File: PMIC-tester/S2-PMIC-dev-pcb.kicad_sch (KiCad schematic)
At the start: 25 parts, among them J1 USB_C_Receptacle_USB2.0, P1 CONN_02X13, P3 CONN_02X13, SW1 RESET, SW2 BOOT, U1 MCP1700-1202E_SOT23, U2 ESP32-S2-WROVER, U3 TPS65185RGZR

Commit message: DRC
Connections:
- net IO36: now also P3.22 (Pin_22)
- net IO37: now also P3.24 (Pin_24)
- no-connect marks 48 -> 46
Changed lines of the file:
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@@
   (no_connect (at 153.67 138.43))
   (no_connect (at 176.53 153.67))
-  (no_connect (at 191.77 135.89))
-  (no_connect (at 194.31 135.89))
   (no_connect (at 83.82 92.71))
   (no_connect (at 83.82 57.15))
@@
     (stroke (width 0) (type default) (color 0 0 0 0))
   )
+  (wire (pts (xy 83.82 64.77) (xy 86.36 64.77))
+    (stroke (width 0) (type default) (color 0 0 0 0))
+  )
+  (wire (pts (xy 120.65 64.77) (xy 116.84 64.77))
+    (stroke (width 0) (type default) (color 0 0 0 0))
+  )
+  (wire (pts (xy 269.24 77.47) (xy 269.24 68.58))
+    (stroke (width 0) (type default) (color 0 0 0 0))
+  )
+  (wire (pts (xy 149.86 106.68) (xy 119.38 106.68))
+    (stroke (width 0) (type default) (color 0 0 0 0))
+  )
+  (wire (pts (xy 120.65 82.55) (xy 116.84 82.55))
+    (stroke (width 0) (type default) (color 0 0 0 0))
+  )
+  (wire (pts (xy 176.53 135.89) (xy 176.53 138.43))
+    (stroke (width 0) (type default) (color 0 0 0 0))
+  )
   (wire (pts (xy 191.77 135.89) (xy 191.77 138.43))
     (stroke (width 0) (type default) (color 0 0 0 0))
   )
-  (wire (pts (xy 83.82 64.77) (xy 86.36 64.77))
-    (stroke (width 0) (type default) (color 0 0 0 0))
-  )
-  (wire (pts (xy 120.65 64.77) (xy 116.84 64.77))
-    (stroke (width 0) (type default) (color 0 0 0 0))
-  )
-  (wire (pts (xy 269.24 77.47) (xy 269.24 68.58))
-    (stroke (width 0) (type default) (color 0 0 0 0))
-  )
-  (wire (pts (xy 149.86 106.68) (xy 119.38 106.68))
-    (stroke (width 0) (type default) (color 0 0 0 0))
-  )
-  (wire (pts (xy 120.65 82.55) (xy 116.84 82.55))
-    (stroke (width 0) (type default) (color 0 0 0 0))
-  )
-  (wire (pts (xy 176.53 135.89) (xy 176.53 138.43))
-    (stroke (width 0) (type default) (color 0 0 0 0))
-  )
   (wire (pts (xy 140.97 116.84) (xy 143.51 116.84))
     (stroke (width 0) (type default) (color 0 0 0 0))
@@
     (stroke (width 0) (type default) (color 0 0 0 0))
   )
+  (wire (pts (xy 256.54 34.29) (xy 262.89 34.29))
+    (stroke (width 0) (type default) (color 0 0 0 0))
+  )
+  (wire (pts (xy 83.82 77.47) (xy 86.36 77.47))
+    (stroke (width 0) (type default) (color 0 0 0 0))
+  )
+  (wire (pts (xy 171.45 151.13) (xy 171.45 161.29))
+    (stroke (width 0) (type default) (color 0 0 0 0))
+  )
+  (wire (pts (xy 120.65 44.45) (xy 116.84 44.45))
+    (stroke (width 0) (type default) (color 0 0 0 0))
+  )
+  (wire (pts (xy 83.82 80.01) (xy 86.36 80.01))
+    (stroke (width 0) (type default) (color 0 0 0 0))
+  )
+  (wire (pts (xy 166.37 135.89) (xy 166.37 138.43))
+    (stroke (width 0) (type default) (color 0 0 0 0))
+  )
+  (wire (pts (xy 160.02 41.91) (xy 162.56 41.91))
+    (stroke (width 0) (type default) (color 0 0 0 0))
+  )
+  (wire (pts (xy 83.82 59.69) (xy 86.36 59.69))
+    (stroke (width 0) (type default) (color 0 0 0 0))
+  )
+  (wire (pts (xy 83.82 54.61) (xy 86.36 54.61))
+    (stroke (width 0) (type default) (color 0 0 0 0))
+  )
+  (wire (pts (xy 120.65 132.08) (xy 120.65 161.29))
+    (stroke (width 0) (type default) (color 0 0 0 0))
+  )
+  (wire (pts (xy 120.65 74.93) (xy 116.84 74.93))
+    (stroke (width 0) (type default) (color 0 0 0 0))
+  )
+  (wire (pts (xy 140.97 92.71) (xy 140.97 100.33))
+    (stroke (width 0) (type default) (color 0 0 0 0))
+  )
+  (wire (pts (xy 196.85 153.67) (xy 196.85 151.13))
+    (stroke (width 0) (type default) (color 0 0 0 0))
+  )
+  (wire (pts (xy 120.65 57.15) (xy 116.84 57.15))
+    (stroke (width 0) (type default) (color 0 0 0 0))
+  )
+  (wire (pts (xy 83.82 82.55) (xy 86.36 82.55))
+    (stroke (width 0) (type default) (color 0 0 0 0))
+  )
+  (wire (pts (xy 196.85 135.89) (xy 196.85 138.43))
+    (stroke (width 0) (type default) (color 0 0 0 0))
+  )
+  (wire (pts (xy 120.65 161.29) (xy 171.45 161.29))
+    (stroke (width 0) (type default) (color 0 0 0 0))
+  )
+  (wire (pts (xy 254 113.03) (xy 254 115.57))
+    (stroke (width 0) (type default) (color 0 0 0 0))
+  )
+  (wire (pts (xy 269.24 33.02) (xy 274.32 33.02))
+    (stroke (width 0) (type default) (color 0 0 0 0))
+  )
+  (wire (pts (xy 149.86 88.9) (xy 149.86 106.68))
+    (stroke (width 0) (type default) (color 0 0 0 0))
+  )
+  (wire (pts (xy 166.37 153.67) (xy 166.37 151.13))
+    (stroke (width 0) (type default) (color 0 0 0 0))
+  )
+  (polyline (pts (xy 176.53 26.67) (xy 138.43 26.67))
+    (stroke (width 0) (type default) (color 0 0 0 0))
+  )
   (wire (pts (xy 194.31 135.89) (xy 194.31 138.43))
-    (stroke (width 0) (type default) (color 0 0 0 0))
-  )
-  (wire (pts (xy 256.54 34.29) (xy 262.89 34.29))
-    (stroke (width 0) (type default) (color 0 0 0 0))
-  )
-  (wire (pts (xy 83.82 77.47) (xy 86.36 77.47))
-    (stroke (width 0) (type default) (color 0 0 0 0))
-  )
-  (wire (pts (xy 171.45 151.13) (xy 171.45 161.29))
-    (stroke (width 0) (type default) (color 0 0 0 0))
-  )
-  (wire (pts (xy 120.65 44.45) (xy 116.84 44.45))
-    (stroke (width 0) (type default) (color 0 0 0 0))
-  )
-  (wire (pts (xy 83.82 80.01) (xy 86.36 80.01))
-    (stroke (width 0) (type default) (color 0 0 0 0))
-  )
-  (wire (pts (xy 166.37 135.89) (xy 166.37 138.43))
-    (stroke (width 0) (type default) (color 0 0 0 0))
-  )
-  (wire (pts (xy 160.02 41.91) (xy 162.56 41.91))
-    (stroke (width 0) (type default) (color 0 0 0 0))
-  )
-  (wire (pts (xy 83.82 59.69) (xy 86.36 59.69))
-    (stroke (width 0) (type default) (color 0 0 0 0))
-  )
-  (wire (pts (xy 83.82 54.61) (xy 86.36 54.61))
-    (stroke (width 0) (type default) (color 0 0 0 0))
-  )
-  (wire (pts (xy 120.65 132.08) (xy 120.65 161.29))
-    (stroke (width 0) (type default) (color 0 0 0 0))
-  )
-  (wire (pts (xy 120.65 74.93) (xy 116.84 74.93))
-    (stroke (width 0) (type default) (color 0 0 0 0))
-  )
-  (wire (pts (xy 140.97 92.71) (xy 140.97 100.33))
-    (stroke (width 0) (type default) (color 0 0 0 0))
-  )
-  (wire (pts (xy 196.85 153.67) (xy 196.85 151.13))
-    (stroke (width 0) (type default) (color 0 0 0 0))
-  )
-  (wire (pts (xy 120.65 57.15) (xy 116.84 57.15))
-    (stroke (width 0) (type default) (color 0 0 0 0))
-  )
-  (wire (pts (xy 83.82 82.55) (xy 86.36 82.55))
-    (stroke (width 0) (type default) (color 0 0 0 0))
-  )
-  (wire (pts (xy 196.85 135.89) (xy 196.85 138.43))
-    (stroke (width 0) (type default) (color 0 0 0 0))
-  )
-  (wire (pts (xy 120.65 161.29) (xy 171.45 161.29))
-    (stroke (width 0) (type default) (color 0 0 0 0))
-  )
-  (wire (pts (xy 254 113.03) (xy 254 115.57))
-    (stroke (width 0) (type default) (color 0 0 0 0))
-  )
-  (wire (pts (xy 269.24 33.02) (xy 274.32 33.02))
-    (stroke (width 0) (type default) (color 0 0 0 0))
-  )
-  (wire (pts (xy 149.86 88.9) (xy 149.86 106.68))
-    (stroke (width 0) (type default) (color 0 0 0 0))
-  )
-  (wire (pts (xy 166.37 153.67) (xy 166.37 151.13))
-    (stroke (width 0) (type default) (color 0 0 0 0))
-  )
-  (polyline (pts (xy 176.53 26.67) (xy 138.43 26.67))
     (stroke (width 0) (type default) (color 0 0 0 0))
   )
@@
     (effects (font (size 1.27 1.27)) (justify left bottom))
   )
+  (label "IO37" (at 194.31 135.89 90)
+    (effects (font (size 1.27 1.27)) (justify left bottom))
+  )
   (label "3.3V" (at 218.44 80.01 180)
     (effects (font (size 1.27 1.27)) (justify right bottom))
@@
     (effects (font (size 1.27 1.27)) (justify left bottom))
   )
+  (label "IO36" (at 191.77 135.89 90)
+    (effects (font (size 1.27 1.27)) (justify left bottom))
+  )

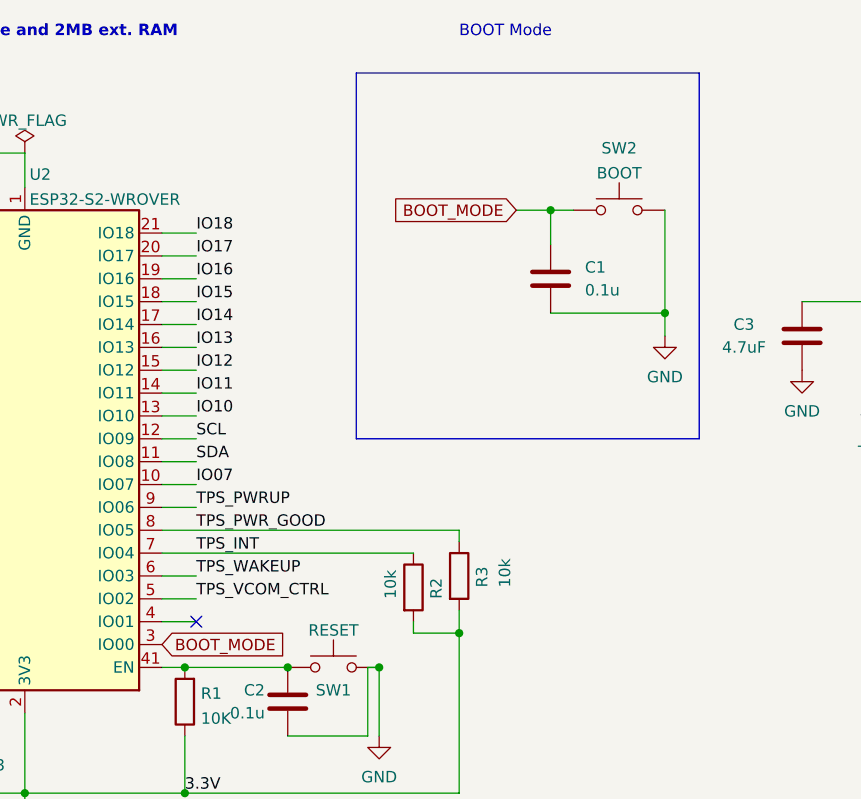
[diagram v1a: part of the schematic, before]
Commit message: I2C pullups
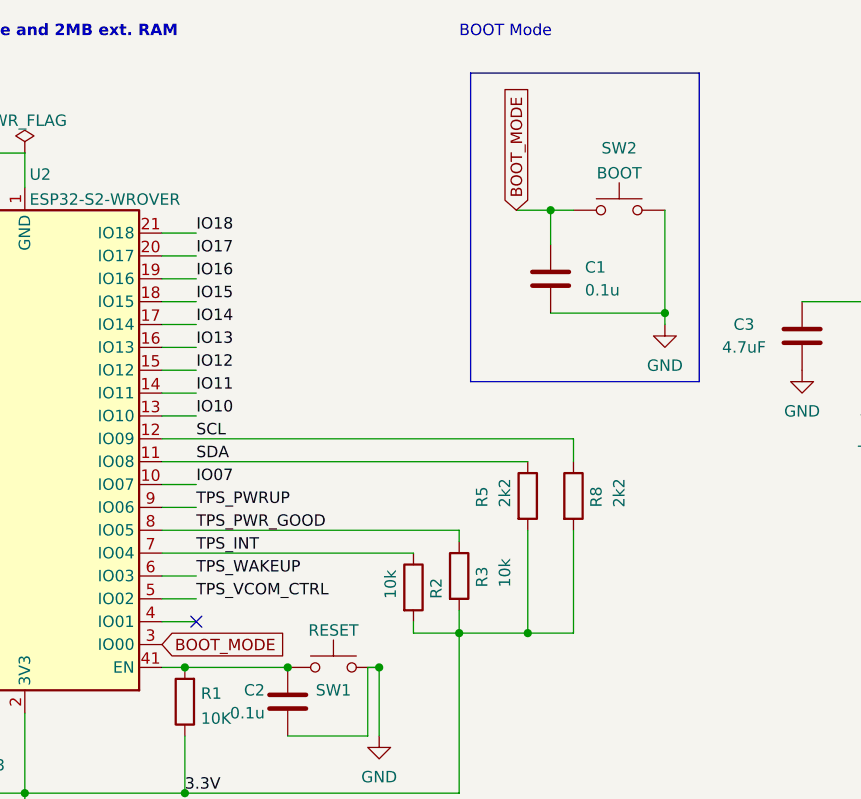
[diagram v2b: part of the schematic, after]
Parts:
- added R5, R8: 2k2, Resistor_SMD:R_0603_1608Metric, symbol Device:R
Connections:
- net 3.3V: now also R5.2, R8.2
- net SCL: now also R8.1
- net SDA: now also R5.1
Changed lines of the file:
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@@
   (junction (at 172.72 53.34) (diameter 0) (color 0 0 0 0)
+  )
+  (junction (at 157.48 88.9) (diameter 0) (color 0 0 0 0)
   )
   (junction (at 52.07 54.61) (diameter 0) (color 0 0 0 0)
@@
     (stroke (width 0) (type default) (color 0 0 0 0))
   )
+  (wire (pts (xy 162.56 67.31) (xy 162.56 69.85))
+    (stroke (width 0) (type default) (color 0 0 0 0))
+  )
   (wire (pts (xy 254 57.15) (xy 276.86 57.15))
     (stroke (width 0) (type default) (color 0 0 0 0))
@@
     (stroke (width 0) (type default) (color 0 0 0 0))
   )
+  (wire (pts (xy 157.48 77.47) (xy 157.48 88.9))
+    (stroke (width 0) (type default) (color 0 0 0 0))
+  )
   (wire (pts (xy 194.31 153.67) (xy 194.31 151.13))
     (stroke (width 0) (type default) (color 0 0 0 0))
@@
     (stroke (width 0) (type default) (color 0 0 0 0))
   )
-  (polyline (pts (xy 138.43 26.67) (xy 138.43 67.31))
+  (polyline (pts (xy 151.13 26.67) (xy 151.13 60.96))
     (stroke (width 0) (type default) (color 0 0 0 0))
   )
@@
     (stroke (width 0) (type default) (color 0 0 0 0))
   )
-  (wire (pts (xy 120.65 69.85) (xy 116.84 69.85))
+  (wire (pts (xy 116.84 69.85) (xy 157.48 69.85))
     (stroke (width 0) (type default) (color 0 0 0 0))
   )
@@
     (stroke (width 0) (type default) (color 0 0 0 0))
   )
+  (wire (pts (xy 162.56 88.9) (xy 157.48 88.9))
+    (stroke (width 0) (type default) (color 0 0 0 0))
+  )
   (wire (pts (xy 269.24 68.58) (xy 274.32 68.58))
     (stroke (width 0) (type default) (color 0 0 0 0))
@@
     (stroke (width 0) (type default) (color 0 0 0 0))
   )
+  (wire (pts (xy 162.56 77.47) (xy 162.56 88.9))
+    (stroke (width 0) (type default) (color 0 0 0 0))
+  )
   (wire (pts (xy 53.34 44.45) (xy 57.15 44.45))
     (stroke (width 0) (type default) (color 0 0 0 0))
@@
     (stroke (width 0) (type default) (color 0 0 0 0))
   )
-  (polyline (pts (xy 176.53 26.67) (xy 138.43 26.67))
+  (polyline (pts (xy 176.53 26.67) (xy 151.13 26.67))
     (stroke (width 0) (type default) (color 0 0 0 0))
   )
@@
     (stroke (width 0) (type default) (color 0 0 0 0))
   )
-  (polyline (pts (xy 138.43 67.31) (xy 176.53 67.31))
+  (polyline (pts (xy 151.13 60.96) (xy 176.53 60.96))
     (stroke (width 0) (type default) (color 0 0 0 0))
   )
@@
     (stroke (width 0) (type default) (color 0 0 0 0))
   )
-  (polyline (pts (xy 176.53 67.31) (xy 176.53 26.67))
+  (polyline (pts (xy 176.53 60.96) (xy 176.53 26.67))
     (stroke (width 0) (type default) (color 0 0 0 0))
   )
@@
     (stroke (width 0) (type default) (color 0 0 0 0))
   )
-  (wire (pts (xy 120.65 67.31) (xy 116.84 67.31))
+  (wire (pts (xy 116.84 67.31) (xy 162.56 67.31))
     (stroke (width 0) (type default) (color 0 0 0 0))
   )
@@
     (stroke (width 0) (type default) (color 0 0 0 0))
   )
-  (wire (pts (xy 172.72 53.34) (xy 172.72 55.88))
+  (wire (pts (xy 172.72 53.34) (xy 172.72 54.61))
     (stroke (width 0) (type default) (color 0 0 0 0))
   )
@@
   )
   (wire (pts (xy 179.07 135.89) (xy 179.07 138.43))
+    (stroke (width 0) (type default) (color 0 0 0 0))
+  )
+  (wire (pts (xy 157.48 88.9) (xy 149.86 88.9))
     (stroke (width 0) (type default) (color 0 0 0 0))
   )
@@
     )
   )
-  (global_label "BOOT_MODE" (shape input) (at 156.21 41.91 180) (fields_autoplaced)
-    (effects (font (size 1.27 1.27)) (justify right))
-    (property "Intersheet References" "${INTERSHEET_REFS}" (id 0) (at 142.5393 41.9894 0)
-      (effects (font (size 1.27 1.27)) (justify right) hide)
+  (global_label "BOOT_MODE" (shape input) (at 156.21 41.91 90) (fields_autoplaced)
+    (effects (font (size 1.27 1.27)) (justify left))
+    (property "Intersheet References" "${INTERSHEET_REFS}" (id 0) (at 156.1306 28.2393 90)
+      (effects (font (size 1.27 1.27)) (justify left) hide)
     )
   )
@@
     (pin "8")
     (pin "9")
+  )
+  (symbol (lib_id "Device:R") (at 157.48 73.66 0) (unit 1)
+    (in_bom yes) (on_board yes)
+    (property "Reference" "R5" (id 0) (at 152.4 74.93 90)
+      (effects (font (size 1.27 1.27)) (justify left))
+    )
+    (property "Value" "2k2" (id 1) (at 154.94 74.93 90)
+      (effects (font (size 1.27 1.27)) (justify left))
+    )
+    (property "Footprint" "Resistor_SMD:R_0603_1608Metric" (id 2) (at 155.702 73.66 90)
+      (effects (font (size 1.27 1.27)) hide)
+    )
+    (property "Datasheet" "~" (id 3) (at 157.48 73.66 0)
+      (effects (font (size 1.27 1.27)) hide)
+    )
+    (property "LCSC" "C25804" (id 4) (at 157.48 73.66 90)
+      (effects (font (size 1.27 1.27)) hide)
+    )
+    (pin "1")
+    (pin "2")
   )
   (symbol (lib_id "Device:LED") (at 147.32 116.84 0) (unit 1)
@@
     (pin "1")
   )
-  (symbol (lib_id "power:GND") (at 172.72 55.88 0) (unit 1)
-    (in_bom yes) (on_board yes) (fields_autoplaced)
-    (property "Reference" "#PWR07" (id 0) (at 172.72 62.23 0)
-      (effects (font (size 1.27 1.27)) hide)
-    )
-    (property "Value" "GND" (id 1) (at 172.72 60.4425 0))
-    (property "Footprint" "" (id 2) (at 172.72 55.88 0)
-      (effects (font (size 1.27 1.27)) hide)
-    )
-    (property "Datasheet" "" (id 3) (at 172.72 55.88 0)
+  (symbol (lib_id "power:GND") (at 172.72 54.61 0) (unit 1)
+    (in_bom yes) (on_board yes) (fields_autoplaced)
+    (property "Reference" "#PWR07" (id 0) (at 172.72 60.96 0)
+      (effects (font (size 1.27 1.27)) hide)
+    )
+    (property "Value" "GND" (id 1) (at 172.72 59.1725 0))
+    (property "Footprint" "" (id 2) (at 172.72 54.61 0)
+      (effects (font (size 1.27 1.27)) hide)
+    )
+    (property "Datasheet" "" (id 3) (at 172.72 54.61 0)
       (effects (font (size 1.27 1.27)) hide)
     )
@@
     (pin "2")
   )
+  (symbol (lib_id "Device:R") (at 162.56 73.66 0) (unit 1)
+    (in_bom yes) (on_board yes)
+    (property "Reference" "R8" (id 0) (at 165.1 74.93 90)
+      (effects (font (size 1.27 1.27)) (justify left))
+    )
+    (property "Value" "2k2" (id 1) (at 167.64 74.93 90)
+      (effects (font (size 1.27 1.27)) (justify left))
+    )
+    (property "Footprint" "Resistor_SMD:R_0603_1608Metric" (id 2) (at 160.782 73.66 90)
+      (effects (font (size 1.27 1.27)) hide)
+    )
+    (property "Datasheet" "~" (id 3) (at 162.56 73.66 0)
+      (effects (font (size 1.27 1.27)) hide)
+    )
+    (property "LCSC" "C25804" (id 4) (at 162.56 73.66 90)
+      (effects (font (size 1.27 1.27)) hide)
+    )
+    (pin "1")
+    (pin "2")
+  )
   (symbol (lib_id "power:GND") (at 138.43 124.46 0) (unit 1)
     (in_bom yes) (on_board yes) (fields_autoplaced)
@@
       (reference "R4") (unit 1) (value "1k") (footprint "Resistor_SMD:R_0603_1608Metric")
     )
+    (path "/08b383c5-1727-4397-94f1-1480b0709625"
+      (reference "R5") (unit 1) (value "2k2") (footprint "Resistor_SMD:R_0603_1608Metric")
+    )
     (path "/6b34b0b7-9744-4931-b6aa-02fd4bc0e4b0"
       (reference "R6") (unit 1) (value "5.1k") (footprint "Resistor_SMD:R_0603_1608Metric")
@@
       (reference "R7") (unit 1) (value "5.1k") (footprint "Resistor_SMD:R_0603_1608Metric")
     )
+    (path "/e9a38284-2143-426d-951f-688589804155"
+      (reference "R8") (unit 1) (value "2k2") (footprint "Resistor_SMD:R_0603_1608Metric")
+    )
     (path "/45a0ac59-ca27-4917-96a0-95d11b16f980"
